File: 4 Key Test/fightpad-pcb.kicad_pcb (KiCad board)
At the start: 2 copper layers, 23 parts, among them SW1 SW_PUSH, U1 ATmega32U4-A, Y1 16MHz

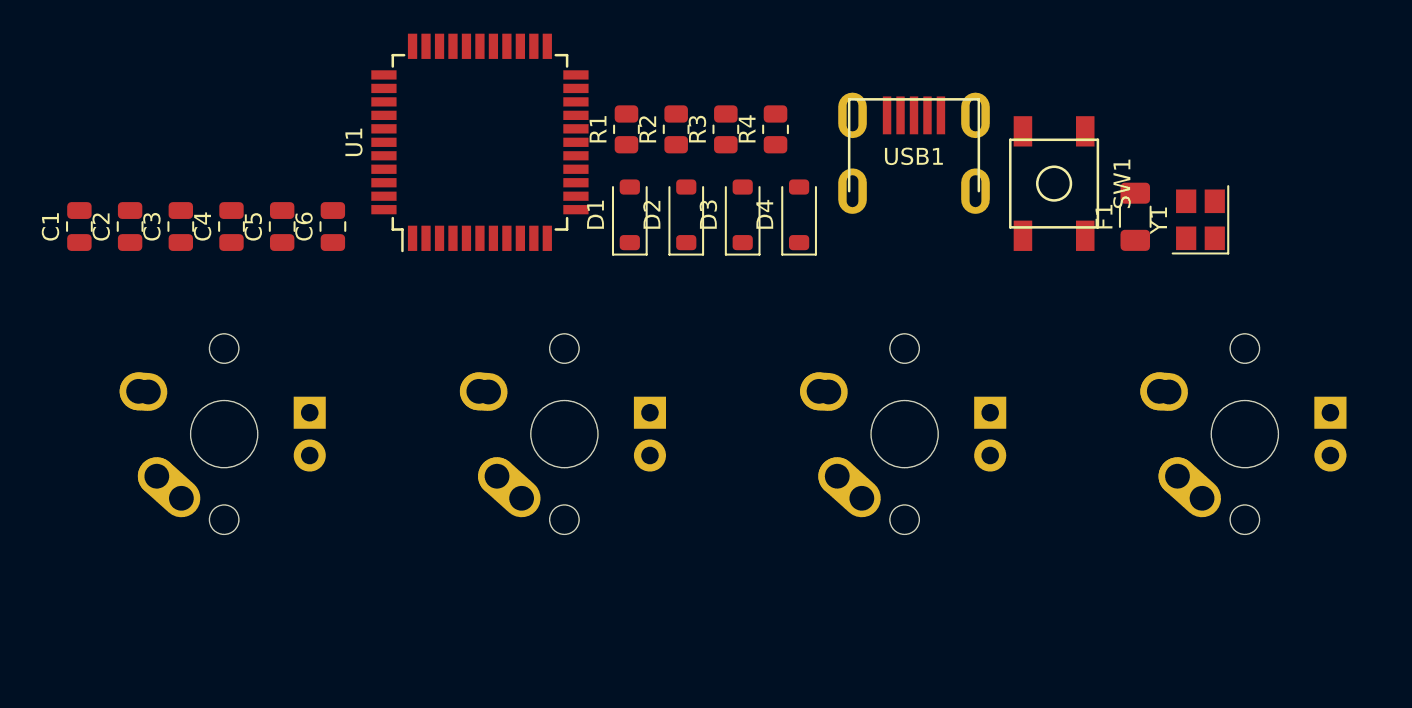
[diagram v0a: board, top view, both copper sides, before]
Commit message: Reorganization
Prep for Pro Micro Based File after Test File Finished
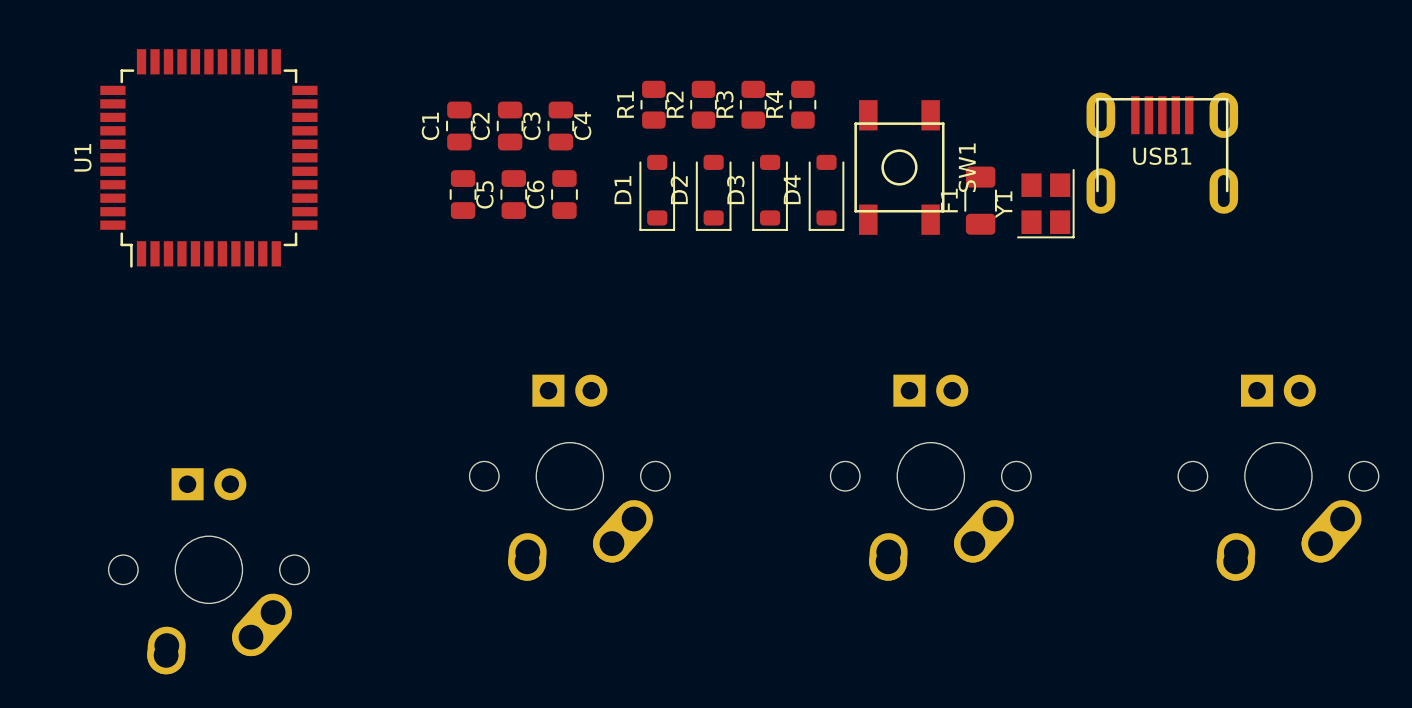
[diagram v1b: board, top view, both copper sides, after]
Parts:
- moved MX4 40.2 mm to (49.2, 61.1), turned to 180 degrees
- moved C1 23.3 mm to (42.7, 40.3)
- moved C2 23.3 mm to (45.7, 40.3)
- moved C3 23.3 mm to (48.7, 40.3)
- moved MX3 22.3 mm to (91.3, 61.1), turned to 180 degrees
- moved MX2 21.9 mm to (70.6, 61.1), turned to 180 degrees
- moved U1 16.1 mm to (27.8, 42.2)
- moved USB1 14.7 mm to (84.4, 44.2)
- moved C4 13.9 mm to (42.9, 44.4)
- moved C5 13.9 mm to (45.9, 44.4)
- moved C6 13.9 mm to (48.9, 44.4)
- moved F1 9.23 mm to (73.6, 44.8)
- moved SW1 9.23 mm to (68.8, 42.8)
- moved Y1 9.23 mm to (77.5, 44.9)
- moved MX1 8.11 mm to (27.8, 66.7), turned to 180 degrees
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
